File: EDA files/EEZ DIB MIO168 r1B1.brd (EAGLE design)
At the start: 146 x 95 mm, 291 parts, among them IC1 M24C32-WMN6P, IC10 DAC7760IPWPR, IC11 DAC7760IPWPR, IC12 OPA376AIDBVR, IC13 DAC7563TDGSR, IC14 OPA2196D, IC15 BTS3408G, IC16 BTS3408G, IC17 BTS3408G, IC18 BTS3408G, IC19 74HC126PW,118, IC2 Si8641AB-B-IS1, IC20 TL431B, IC21 DG468DV-T1-E3, IC22 DG468DV-T1-E3, IC23 DG468DV-T1-E3, IC24 DG468DV-T1-E3, IC25 DG468DV-T1-E3, IC26 DG468DV-T1-E3, IC27 DG468DV-T1-E3, IC28 DG468DV-T1-E3, IC29 DG468DV-T1-E3, IC3 Si8641AB-B-IS1, IC30 DG468DV-T1-E3, IC31 DG468DV-T1-E3, IC32 DG468DV-T1-E3, IC33 DG468DV-T1-E3, IC34 DG468DV-T1-E3, IC35 OPA376AIDBVR, IC36 ADS8674IDBT, IC4 MC78L12, IC5 LP2985-5DBVR, IC6 LP2985-33DBVR, IC7 MC79L12, IC8 STM32F446ZCT6, IC9 OPA2196D, J1 4907, J2 503398-1892, Q1 2N7002PS, Q10 BSS169, Q11 BSS169, Q12 BSS169, Q13 BSS169, Q2 2N7002PS, Q3 2N7002PS, Q4 2N7002PS, Q5 2N7002PS, Q6 BSS169, Q7 BSS169, Q8 BSS169, Q9 BSS169, X1 77317-104-28LF, X2 SSW-106-02-S-S, X3 691327310016, X4 691327310016, Y1 25MHz

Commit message: BOM added
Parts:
- C16, C18, C21: device rcl:C1206 -> rcl:C0805
- C75: device rcl:C1210 -> rcl:C1206
- IC14, IC9: value OPA2196D -> OPA2196IDR
- IC2, IC3: value Si8641AB-B-IS1 -> Si8641BB-B-IS1
- IC4: value MC78L12 -> L78L12
- IC5: value LP2985-5DBVR -> LP2985-50DBVR
- IC7: value MC79L12 -> L79L12
- TVS1, TVS2, TVS3, TVS4, TVS5, TVS6, TVS7, TVS8: value PESD12VL1BA.115 -> PESD12VL1BA,115
- moved C74 0.76 mm to (83.0, 88.8)
- moved C21 0.51 mm to (127.1, 89.3)
- moved C18 0.34 mm to (138.0, 42.9)
- moved C75 0.32 mm to (81.0, 89.6)
- moved C16 0.14 mm to (138.0, 41.0)
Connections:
- removed net +5V: X1.23, X1.24
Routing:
- net +5V_ISO: track 162.2 -> 163.3 mm
- net +3V3_ISO: track 52.7 -> 53.3 mm, vias 19 -> 20

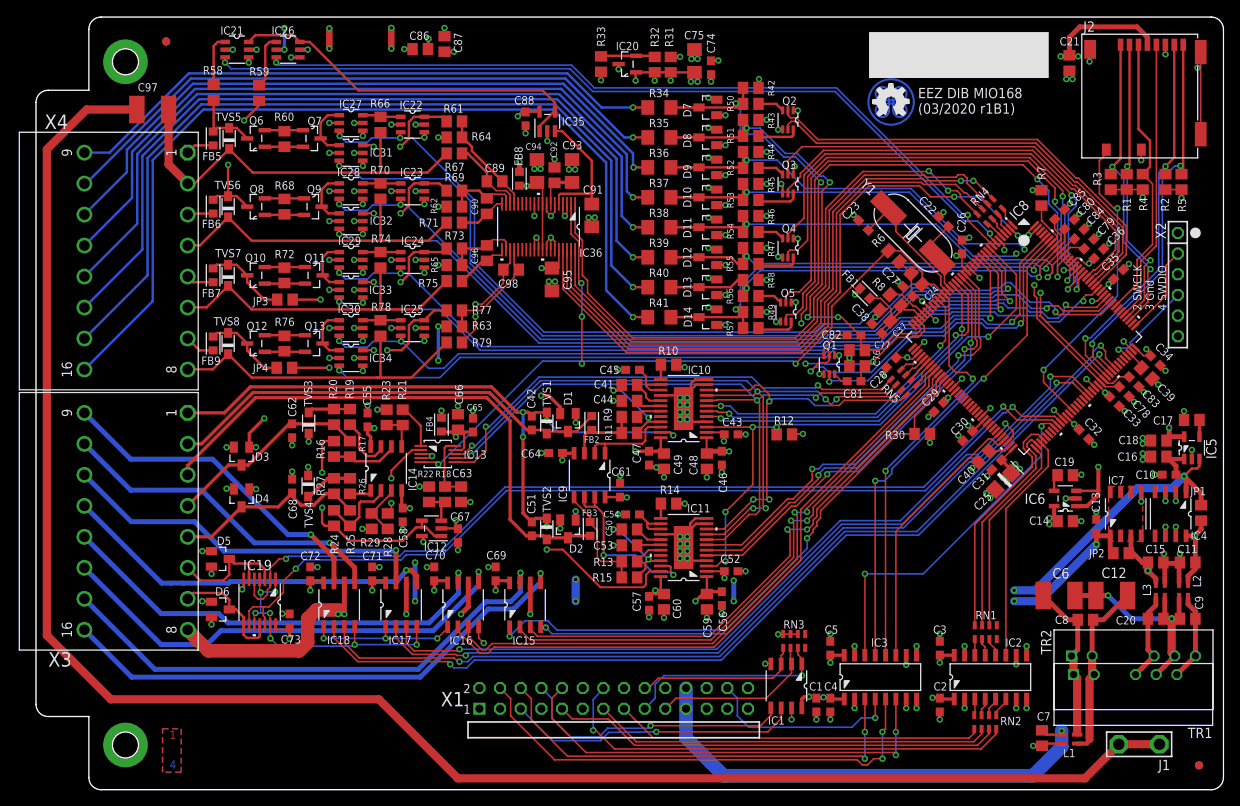
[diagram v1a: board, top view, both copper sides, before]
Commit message: PWM outputs clamp fix
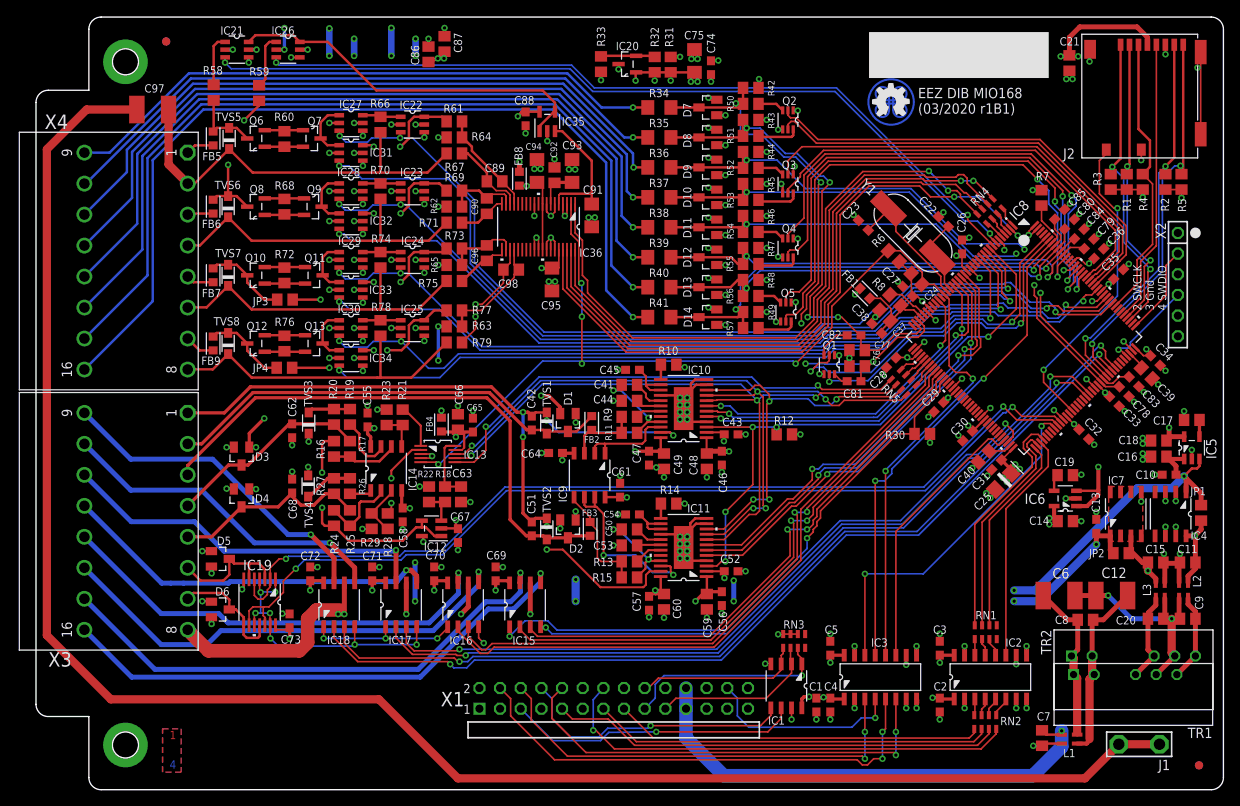
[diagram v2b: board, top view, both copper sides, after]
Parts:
- moved C86 1.20 mm to (48.3, 90.4), turned to 270 degrees
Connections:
- net +5V_ISO: now also D5.2, D6.2
- net CLAMP: no longer D5.2, D6.2
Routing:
- net +5V_ISO: track 163.3 -> 270.7 mm, vias 3 -> 5
- net CLAMP: track 120.6 -> 19.7 mm, vias 16 -> 14
- net CURR_SW0: track 117.0 -> 116.3 mm
- net VOLT_SW0: track 104.7 -> 104.2 mm
- net +15V_ISO: track 273.7 -> 273.3 mm, vias 16 -> 20

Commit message: Vref selection for NTC bias (JP3)
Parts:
- added JP5: JP2-CUT-0805, EEZ_Lib1:R_0805
- JP3: value JP2-CUT-0805 -> JP3-CUT; device EEZ_Lib1:R_0805 -> EEZ_Lib1:JP3-CUT
- moved JP3 27.1 mm to (37.6, 86.5), turned to 180 degrees
- moved JP4 8.38 mm to (30.6, 60.3)
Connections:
- new net N$20: IC21.6, IC26.6, JP3.COM
- net 1V25_REF: now also JP3.NO
- net N$136: now also JP4.1; no longer JP3.1
- net N$137: now also JP5.1; no longer JP4.1
- net N$28: now also JP5.2; no longer JP4.2
- net N$31: now also JP3.NC; no longer IC21.6, IC26.6
- net N$87: now also JP4.2; no longer JP3.2
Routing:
- net 1V25_REF: track 28.9 -> 74.9 mm, vias 2 -> 4
- net N$20: track 0.00 -> 16.6 mm
- net N$31: track 45.8 -> 30.0 mm
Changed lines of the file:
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@@
 <layer number="27" name="tValues" color="14" fill="1" visible="no" active="yes"/>
 <layer number="28" name="bValues" color="10" fill="1" visible="no" active="yes"/>
-<layer number="29" name="tStop" color="7" fill="1" visible="no" active="yes"/>
+<layer number="29" name="tStop" color="7" fill="1" visible="yes" active="yes"/>
 <layer number="30" name="bStop" color="7" fill="1" visible="no" active="yes"/>
 <layer number="31" name="tCream" color="7" fill="4" visible="no" active="yes"/>
@@
 <attribute name="VALUE" x="64.897" y="33.782" size="0.6096" layer="27" ratio="10" rot="R270"/>
 </element>
-<element name="JP3" library="EEZ_Lib1" package="R_0805" value="JP2-CUT-0805" x="30.607" y="60.2615" smashed="yes">
+<element name="JP4" library="EEZ_Lib1" package="R_0805" value="JP2-CUT-0805" x="30.607" y="60.2615" smashed="yes">
 <attribute name="NAME" x="28.575" y="60.579" size="1.016" layer="25" ratio="10" rot="R180"/>
 <attribute name="VALUE" x="30.607" y="60.2615" size="0.6096" layer="27" ratio="10" align="center"/>
 </element>
-<element name="JP4" library="EEZ_Lib1" package="R_0805" value="JP2-CUT-0805" x="30.5435" y="51.8795" smashed="yes">
+<element name="JP5" library="EEZ_Lib1" package="R_0805" value="JP2-CUT-0805" x="30.5435" y="51.8795" smashed="yes">
 <attribute name="NAME" x="28.575" y="52.3875" size="1.016" layer="25" ratio="10" rot="R180"/>
 <attribute name="VALUE" x="30.5435" y="51.8795" size="0.6096" layer="27" ratio="10" align="center"/>
 </element>
+<element name="JP3" library="EEZ_Lib1" package="JP3-CUT" value="JP3-CUT" x="37.592" y="86.487" smashed="yes" rot="R180">
+<attribute name="NAME" x="36.5125" y="87.503" size="0.8128" layer="25" ratio="10"/>
+</element>
 </elements>
 <signals>
@@
 <wire x1="137.099" y1="40.9575" x2="136.4615" y2="40.9575" width="0.6096" layer="1"/>
 <wire x1="136.4615" y1="40.9575" x2="136.0805" y2="41.3385" width="0.6096" layer="1"/>
-<wire x1="18.6785" y1="74.549" x2="18.65" y2="74.525" width="0" layer="19" extent="1-1"/>
+<wire x1="50.2285" y1="90.744" x2="50.2285" y2="89.9795" width="0.3048" layer="1"/>
+<wire x1="50.2285" y1="89.9795" x2="50.165" y2="89.916" width="0.3048" layer="1"/>
+<wire x1="18.65" y1="74.525" x2="18.6785" y2="74.549" width="0" layer="19" extent="1-1"/>
 <wire x1="18.6785" y1="66.929" x2="18.65" y2="66.905" width="0" layer="19" extent="1-1"/>
 <wire x1="18.6785" y1="59.309" x2="18.65" y2="59.285" width="0" layer="19" extent="1-1"/>
 <wire x1="18.742" y1="51.689" x2="18.65" y2="51.665" width="0" layer="19" extent="1-1"/>
-<wire x1="50.2285" y1="90.744" x2="50.2285" y2="89.9795" width="0.3048" layer="1"/>
-<wire x1="50.2285" y1="89.9795" x2="50.165" y2="89.916" width="0.3048" layer="1"/>
 </signal>
 <signal name="DIB_A0">
@@
 <via x="35.179" y="38.989" extent="1-16" drill="0.4" shape="octagon"/>
 <wire x1="36.6395" y1="32.451" x2="35.499" y2="32.451" width="0.3048" layer="1"/>
-<wire x1="36.6395" y1="42.86" x2="35.499" y2="42.86" width="0.3048" layer="1"/>
+<wire x1="36.6395" y1="42.86" x2="35.1815" y2="42.86" width="0.3048" layer="1"/>
 <wire x1="38.481" y1="30.607" x2="36.6395" y2="32.4485" width="0.3048" layer="1"/>
 <wire x1="36.6395" y1="32.451" x2="36.6395" y2="32.4485" width="0.3048" layer="1"/>
-<wire x1="35.179" y1="38.989" x2="35.179" y2="42.54" width="0.3048" layer="1"/>
-<wire x1="35.179" y1="42.54" x2="35.499" y2="42.86" width="0.3048" layer="1"/>
+<wire x1="35.179" y1="38.989" x2="35.179" y2="42.8625" width="0.3048" layer="1"/>
 <wire x1="35.179" y1="34.671" x2="35.179" y2="32.771" width="0.3048" layer="1"/>
 <wire x1="35.179" y1="32.771" x2="35.499" y2="32.451" width="0.3048" layer="1"/>
+<contactref element="JP3" pad="NO"/>
+<wire x1="36.1315" y1="86.487" x2="34.798" y2="86.487" width="0.3048" layer="1"/>
+<wire x1="34.798" y1="86.487" x2="34.036" y2="85.725" width="0.3048" layer="1"/>
+<via x="34.036" y="82.677" extent="1-16" drill="0.4" shape="octagon"/>
+<wire x1="34.036" y1="82.677" x2="34.036" y2="44.3865" width="0.3048" layer="16"/>
+<wire x1="34.036" y1="44.3865" x2="35.1155" y2="43.4975" width="0.3048" layer="16"/>
+<wire x1="34.036" y1="85.725" x2="34.036" y2="82.677" width="0.3048" layer="1"/>
+<via x="35.179" y="42.8625" extent="1-16" drill="0.4" shape="octagon"/>
+<wire x1="35.179" y1="42.8625" x2="35.179" y2="43.434" width="0.3048" layer="16"/>
+<wire x1="35.179" y1="43.434" x2="35.1155" y2="43.4975" width="0.3048" layer="16"/>
+<wire x1="35.1815" y1="42.86" x2="35.179" y2="42.8625" width="0.3048" layer="1"/>
 </signal>
 <signal name="N$60">
@@
 <contactref element="IC35" pad="4"/>
 <contactref element="IC35" pad="1"/>
-<contactref element="IC21" pad="6"/>
-<contactref element="IC26" pad="6"/>
 <wire x1="63.815" y1="83.3628" x2="63.815" y2="84.4575" width="0.3048" layer="1"/>
-<wire x1="63.815" y1="84.4575" x2="62.2935" y2="85.979" width="0.3048" layer="1"/>
-<wire x1="32.438340625" y1="91.948" x2="32.4358" y2="91.945459375" width="0.3048" layer="1"/>
-<wire x1="26.1493" y1="91.945459375" x2="26.159459375" y2="91.945459375" width="0.3048" layer="1"/>
-<wire x1="26.159459375" y1="91.945459375" x2="26.9875" y2="92.7735" width="0.3048" layer="1"/>
-<wire x1="26.9875" y1="92.7735" x2="31.607759375" y2="92.7735" width="0.3048" layer="1"/>
-<wire x1="31.607759375" y1="92.7735" x2="32.4358" y2="91.945459375" width="0.3048" layer="1"/>
+<wire x1="63.815" y1="84.4575" x2="61.7855" y2="86.487" width="0.3048" layer="1"/>
 <wire x1="61.915" y1="80.9752" x2="61.915" y2="81.6" width="0.3048" layer="1"/>
 <wire x1="61.915" y1="81.6" x2="63.6778" y2="83.3628" width="0.3048" layer="1"/>
 <wire x1="63.815" y1="83.3628" x2="63.6778" y2="83.3628" width="0.3048" layer="1"/>
-<wire x1="32.4358" y1="91.945459375" x2="35.880040625" y2="91.945459375" width="0.3048" layer="1"/>
-<wire x1="35.880040625" y1="91.945459375" x2="41.8465" y2="85.979" width="0.3048" layer="1"/>
-<wire x1="62.2935" y1="85.979" x2="41.8465" y2="85.979" width="0.3048" layer="1"/>
+<contactref element="JP3" pad="NC"/>
+<wire x1="39.0525" y1="86.487" x2="61.7855" y2="86.487" width="0.3048" layer="1"/>
 </signal>
 <signal name="AIN_0P">
@@
 <wire x1="23.622" y1="64.546" x2="22.2305" y2="64.546" width="0.3048" layer="1"/>
 <wire x1="22.2305" y1="64.546" x2="21.7805" y2="64.096" width="0.3048" layer="1"/>
-<contactref element="JP3" pad="1"/>
+<contactref element="JP4" pad="1"/>
 <wire x1="29.657" y1="60.2615" x2="28.067" y2="60.2615" width="0.3048" layer="1"/>
 <wire x1="28.067" y1="60.2615" x2="25.9715" y2="62.357" width="0.3048" layer="1"/>
@@
 <wire x1="23.622" y1="56.164" x2="22.2305" y2="56.164" width="0.3048" layer="1"/>
 <wire x1="22.2305" y1="56.164" x2="21.7805" y2="55.714" width="0.3048" layer="1"/>
-<contactref element="JP4" pad="1"/>
+<contactref element="JP5" pad="1"/>
 <wire x1="29.5935" y1="51.8795" x2="28.067" y2="51.8795" width="0.3048" layer="1"/>
 <wire x1="28.067" y1="51.8795" x2="25.9715" y2="53.975" width="0.3048" layer="1"/>
@@
 <wire x1="50.485" y1="58.928" x2="48.948340625" y2="58.928" width="0.3048" layer="1"/>
 <wire x1="48.948340625" y1="58.928" x2="47.7393" y2="57.718959375" width="0.3048" layer="1"/>
-<contactref element="JP4" pad="2"/>
+<contactref element="JP5" pad="2"/>
 <wire x1="31.4935" y1="51.8795" x2="36.068" y2="51.8795" width="0.3048" layer="1"/>
 <via x="36.068" y="51.8795" extent="1-16" drill="0.4" shape="octagon"/>
@@
 <wire x1="47.7393" y1="66.100959375" x2="50.037959375" y2="66.100959375" width="0.3048" layer="1"/>
 <wire x1="50.037959375" y1="66.100959375" x2="50.485" y2="66.548" width="0.3048" layer="1"/>
-<contactref element="JP3" pad="2"/>
+<contactref element="JP4" pad="2"/>
 <wire x1="31.557" y1="60.2615" x2="34.9885" y2="60.2615" width="0.3048" layer="1"/>
 <via x="34.9885" y="60.2615" extent="1-16" drill="0.4" shape="octagon"/>
@@
 </polygon>
 </signal>
+<signal name="N$20">
+<contactref element="IC26" pad="6"/>
+<contactref element="IC21" pad="6"/>
+<contactref element="JP3" pad="COM"/>
+<wire x1="37.592" y1="86.487" x2="37.592" y2="90.3605" width="0.3048" layer="1"/>
+<wire x1="37.592" y1="90.3605" x2="36.007040625" y2="91.945459375" width="0.3048" layer="1"/>
+<wire x1="32.4358" y1="91.945459375" x2="36.007040625" y2="91.945459375" width="0.3048" layer="1"/>
+<wire x1="26.1493" y1="91.945459375" x2="26.413459375" y2="91.945459375" width="0.3048" layer="1"/>
+<wire x1="26.413459375" y1="91.945459375" x2="27.1145" y2="92.6465" width="0.3048" layer="1"/>
+<wire x1="27.1145" y1="92.6465" x2="31.734759375" y2="92.6465" width="0.3048" layer="1"/>
+<wire x1="31.734759375" y1="92.6465" x2="32.4358" y2="91.945459375" width="0.3048" layer="1"/>
+</signal>
 </signals>

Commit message: Changes suggested by @jbb
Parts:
- added R80, R81: 560K, rcl:R1206
- added R82: 100R, rcl:R0805
- added R83: 1K1, rcl:R0805
- C97: value 4n7/1kV -> 2n2; device rcl:C1812 -> rcl:C0805
- C98: value 2n2 -> 4n7/1kV; device rcl:C0805 -> rcl:C1812
- R31, R70, R74, R78: value 100R -> 47R
- R32: value 470R -> 47R
- R33: value 1K8 -> 100R
- R34: value 2K7 -> 470R; device rcl:R1206 -> rcl:R0805
- R35: value 2K7 -> 1K8; device rcl:R1206 -> rcl:R0805
- R42, R43: value 27K -> 2K7; device rcl:R0805 -> rcl:R1206
- R50, R51: value 1K -> 27K
- R58, R59: value 10K -> 1K
- R60: value 47R -> 10K
- R61: value 1K -> 10K
- R62: value N.C. -> 47R
- R63: value N.C. -> 1K
- R66: value 100R -> N.C.
- R67: value 1K1 -> N.C.
- R68, R72, R76: value 47R -> 100R
- R69, R73, R77: value 1K -> 1K1
- R71, R75, R79: value 1K1 -> 1K
- moved R32 84.5 mm to (22.6, 23.7), turned to 0 degrees
- moved R31 83.4 mm to (22.6, 26.8), turned to 0 degrees
- moved R58 70.6 mm to (87.9, 60.7), turned to 0 degrees
- moved R59 67.0 mm to (87.9, 56.8), turned to 0 degrees
- moved C98 50.6 mm to (11.6, 83.2)
- moved C97 48.3 mm to (58.4, 63.9)
- moved R42 27.0 mm to (76.6, 61.8), turned to 0 degrees
- moved R43 26.7 mm to (76.6, 58.1), turned to 0 degrees
- moved R63 25.2 mm to (51.4, 82.2)
- moved R61 24.3 mm to (27.4, 85.7), turned to 270 degrees
- moved R62 22.5 mm to (30.5, 80.0), turned to 90 degrees
- moved R51 21.7 mm to (87.9, 58.7), turned to 180 degrees
- moved R50 21.7 mm to (87.9, 62.7), turned to 180 degrees
- moved R72 15.7 mm to (42.4, 73.6)
- moved R76 15.7 mm to (42.4, 65.2)
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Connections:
- new net N$21: R80.2, R81.1
- new net N$22: R31.1, X3.6
- new net N$25: R32.1, X3.7
- net +3V3_ISO: now also R33.1; no longer R31.1
- net -12V_ISO: now also R66.1, R67.1; no longer R62.1, R63.1
- net AGND2: now also R72.1, R73.1; no longer R70.1, R71.1
- net AGND4: now also R82.1, R83.1; no longer R78.1, R79.1
- net AIN0: now also R60.2; no longer R58.2
- net AIN1: now also R61.2; no longer R59.2
- net AIN_0GND: now also R69.2; no longer R67.2
- net AIN_0P: now also R63.2, R66.2; no longer R61.2, R64.2
- net AIN_1GND: now also R73.2; no longer R71.2
- net AIN_1P: now also R64.2, R71.2; no longer R62.2, R69.2
- net AIN_2GND: now also R77.2; no longer R75.2
- net AIN_2P: now also R67.2, R75.2; no longer R65.2, R73.2
- net AIN_3GND: now also C97.1, R83.2; no longer C98.1, R79.2
- net AIN_3P: now also C97.2, R65.2, R79.2; no longer C98.2, R63.2, R77.2
- net CLAMP: now also R33.2, R34.1; no longer R31.2, R32.1
- net DIN0: now also R36.2, R44.2, R52.1; no longer R34.2, R42.2, R50.1
- net DIN1: now also R37.2, R45.2, R53.1; no longer R35.2, R43.2, R51.1
- net DIN2: now also R38.2, R46.2, R54.1; no longer R36.2, R44.2, R52.1
- net DIN3: now also R39.2, R47.2, R55.1; no longer R37.2, R45.2, R53.1
- net DIN4: now also R40.2, R48.2, R56.1; no longer R38.2, R46.2, R54.1
- net DIN5: now also R41.2, R49.2, R57.1; no longer R39.2, R47.2, R55.1
- net DIN6: now also R42.2, R50.2, R58.1; no longer R40.2, R48.2, R56.1
- net DIN7: now also R43.2, R51.2, R59.1; no longer R41.2, R49.2, R57.1
- net GND: now also C98.2, R35.2, R50.1, R51.1, R81.2; no longer C97.2, R33.2, R42.1, R43.1
- net N$10: now also R54.2; no longer R52.2
- net N$109: now also R40.1; no longer R38.1
- net N$119: now also R42.1; no longer R40.1
- net N$120: now also R43.1; no longer R41.1
- net N$122: now also R41.1; no longer R39.1
- net N$126: now also R60.1; no longer R58.1
- net N$129: now also R31.2; no longer X3.6
- net N$13: now also R55.2; no longer R53.2
- net N$130: now also R61.1; no longer R59.1
- net N$134: now also R32.2; no longer X3.7
- net N$14: now also R37.1; no longer R35.1
- net N$15: now also R56.2; no longer R54.2
- net N$16: now also R57.2; no longer R55.2
- net N$17: now also R58.2; no longer R56.2
- net N$2: now also R78.1; no longer R76.1
- net N$23: now also R59.2; no longer R57.2
- net N$28: now also R79.1; no longer R77.1
- net N$3: now also R68.1, R69.1; no longer R66.1, R67.1
- net N$32: now also R70.1; no longer R68.1
- net N$33: now also R70.2; no longer R68.2
- net N$36: now also R36.1; no longer R34.1
- net N$38: now also R38.1; no longer R36.1
- net N$4: now also R78.2; no longer R76.2
- net N$42: now also R39.1; no longer R37.1
- net N$50: now also R72.2; no longer R70.2
- net N$51: now also R71.1; no longer R69.1
- net N$6: now also R82.2; no longer R78.2
- net N$7: now also R34.2, R35.1; no longer R32.2, R33.1
- net N$77: now also R74.1; no longer R72.1
- net N$78: now also R62.1; no longer R60.1
- net N$8: now also R52.2; no longer R50.2
- net N$84: now also R74.2; no longer R72.2
- net N$85: now also R76.2; no longer R74.2
- net N$86: now also R62.2; no longer R60.2
- net N$87: now also R75.1; no longer R73.1
- net N$89: now also R68.2; no longer R66.2
- net N$9: now also R53.2; no longer R51.2
- net N$90: now also R76.1, R77.1; no longer R74.1, R75.1
- net N$92: now also R63.1; no longer R61.1
- net PE: now also C98.1, R80.1; no longer C97.1
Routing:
- net GND: track 275.9 -> 282.7 mm
- net PE: track 218.7 -> 213.7 mm, vias 0 -> 2
- net N$134: track 14.9 -> 10.0 mm
- net N$129: track 16.1 -> 12.7 mm
- net N$22: track 0.00 -> 3.21 mm
- net N$25: track 0.00 -> 3.12 mm
- net N$21: track 0.00 -> 2.11 mm
- net N$74: track 25.1 -> 26.8 mm
- net +12V_ISO: track 258.6 -> 260.0 mm
- net +5V_ISO: track 270.7 -> 271.9 mm
- net -12V_ISO: track 262.4 -> 263.3 mm
- net N$126: track 6.39 -> 7.13 mm
